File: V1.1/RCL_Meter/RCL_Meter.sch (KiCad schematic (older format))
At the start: 13 parts

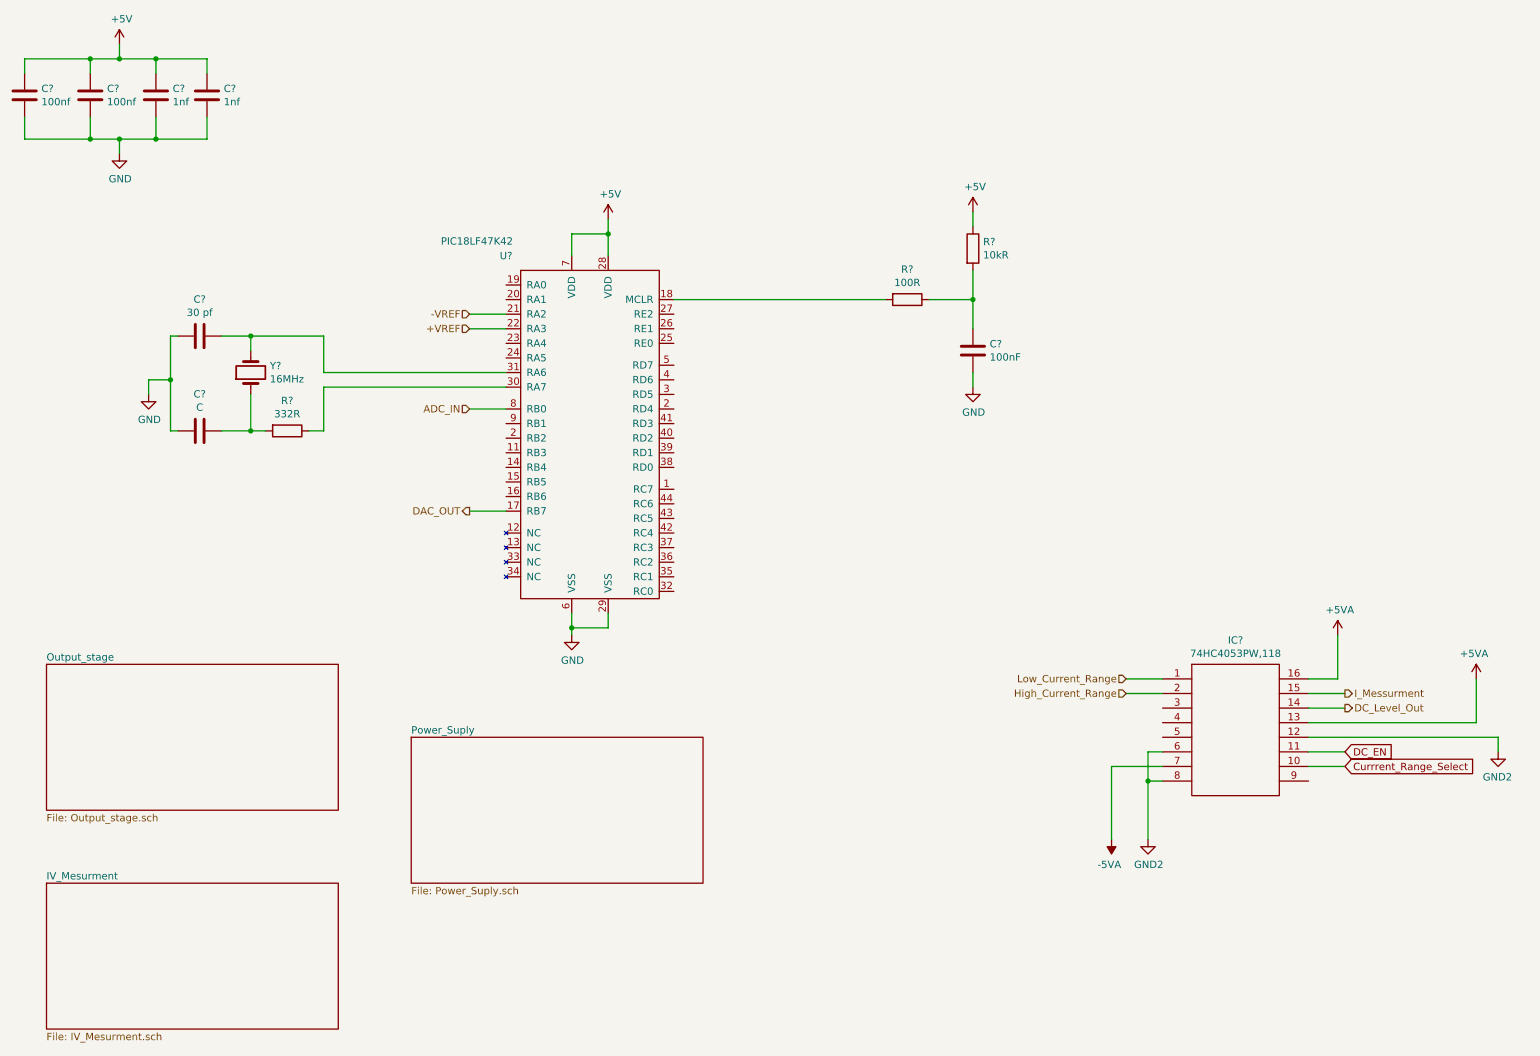
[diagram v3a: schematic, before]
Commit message: Added USB Support
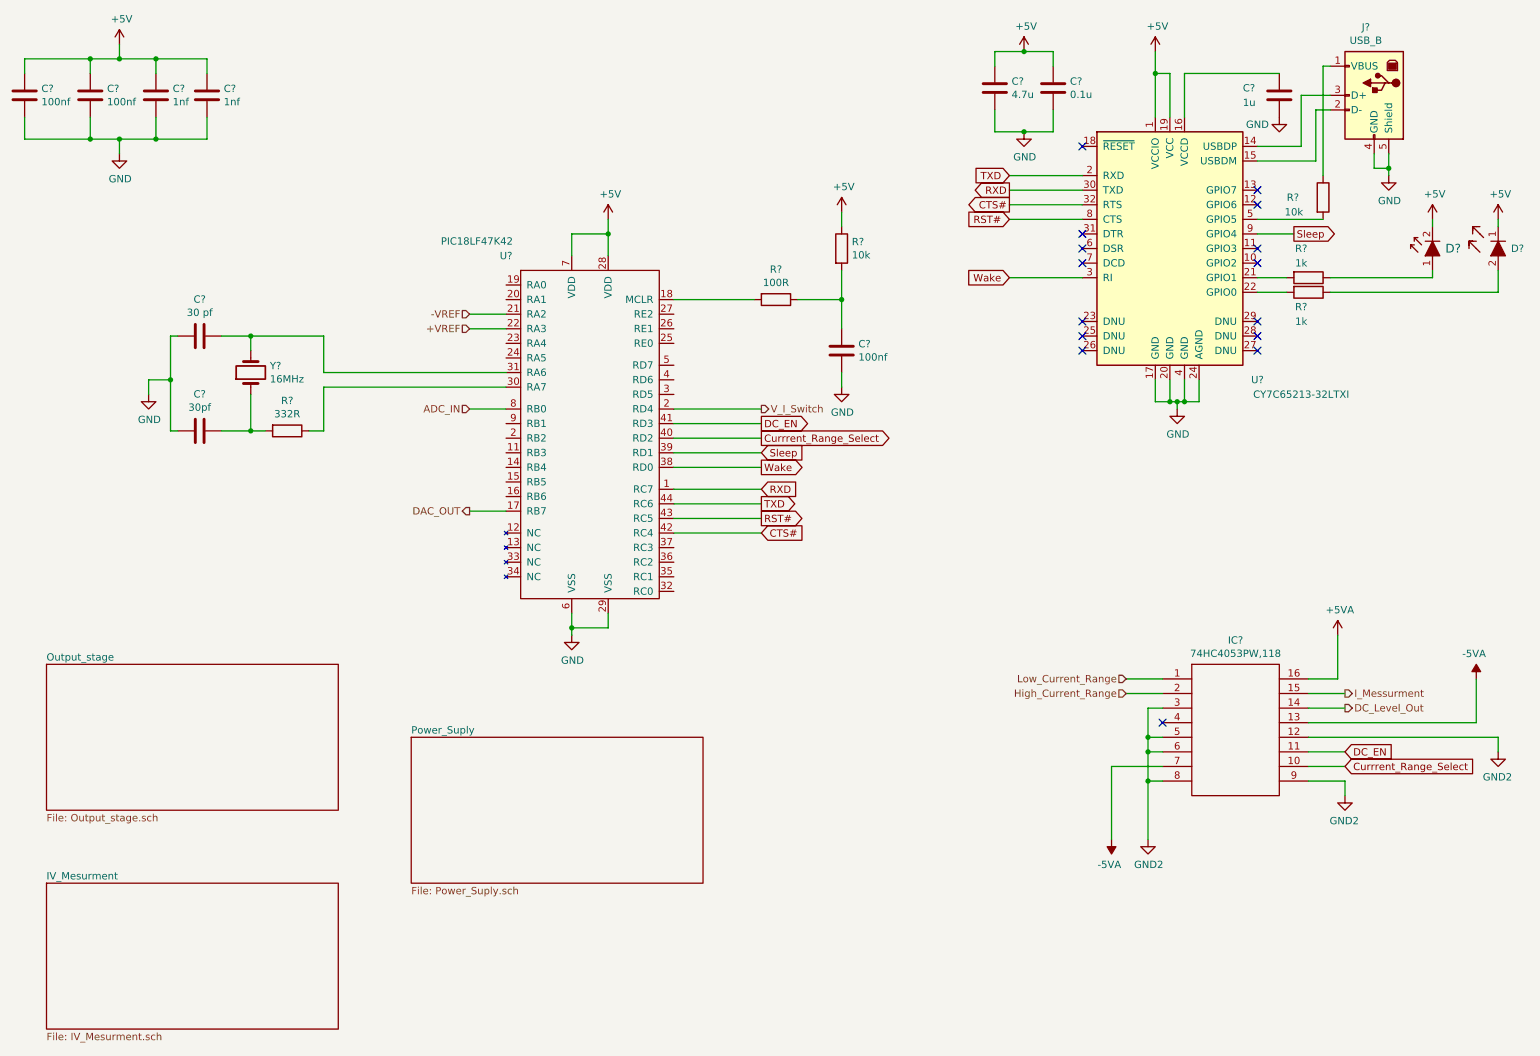
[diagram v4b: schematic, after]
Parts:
- added C?: 1u, symbol Device:C
- added C?: 4.7u, symbol Device:C
- added C?: 0.1u, symbol Device:C
- added D?: LTST-C190KRKT, digikey-footprints:0603, symbol dk_LED-Indication-Discrete:LTST-C190KRKT
- added D?: LTST-C190KGKT, digikey-footprints:LED_0603, symbol dk_LED-Indication-Discrete:LTST-C190KGKT
- added J?: USB_B, symbol Connector:USB_B
- added R?: 10k, symbol Device:R
- added R? (x2): 1k, symbol Device:R
- added U?: CY7C65213-32LTXI, Package_DFN_QFN:QFN-32-1EP_5x5mm_P0.5mm_EP3.45x3.45mm, symbol Interface_USB:CY7C65213-32LTXI
- C?: value 100nF -> 100nf
- C?: value C -> 30pf
- R?: value 10kR -> 10k
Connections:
- net +5V: now also C?.1, C?.1, D?.1, D?.2, U?.1 (VCCIO), U?.19 (VCC)
- net +5VA: no longer IC?.13
- net -5VA: now also IC?.13
- net Currrent_Range_Select: now also U?.40 (RD2)
- net DC_EN: now also U?.41 (RD3)
- net GND: now also C?.2, C?.2, C?.2, J?.4 (GND), J?.5 (Shield), U?.17 (GND), U?.20 (GND), U?.24 (AGND), U?.4 (GND)
- net GND2: now also IC?.3, IC?.5, IC?.9
- net RXD: now reaches U?.1 (RC7)
- net RXD: now also U?.30 (TXD)
- net V_I_Switch: now reaches U?.2 (RD4)
- net Wake: now reaches U?.38 (RD0)
- net Wake: now also U?.3 (RI)
- net Sleep: now reaches U?.39 (RD1)
- net Sleep: now also U?.9 (GPIO4)
- net CTS#: now reaches U?.42 (RC4)
- net CTS#: now also U?.32 (RTS)
- net RST#: now reaches U?.43 (RC5)
- net RST#: now also U?.8 (CTS)
- net TXD: now reaches U?.44 (RC6)
- net TXD: now also U?.2 (RXD)
- new net: J?.3 (D+), U?.14 (USBDP)
- new net: J?.2 (D-), U?.15 (USBDM)
- new net: C?.1, U?.16 (VCCD)
- new net: R?.2, U?.21 (GPIO1)
- new net: R?.2, U?.22 (GPIO0)
- new net: R?.2, U?.5 (GPIO5)
- new net: J?.1 (VBUS), R?.1
- new net: D?.1, R?.1
- new net: D?.2, R?.1
- no-connect marks 0 -> 15
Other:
- moved on the sheet: C?, R?
